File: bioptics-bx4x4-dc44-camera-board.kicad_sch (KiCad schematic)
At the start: 93 parts, among them J3 USB_C_Receptacle_USB2.0, J4 TagConnect_TC2030_SWD, U10 SRV05-4, U11 IS4xS32160F-xTL, U12 USB3300-EZK, U13 AMS1117-3.3, U14 STM32H753IITx, U9 FP6291, Y1 24MHz

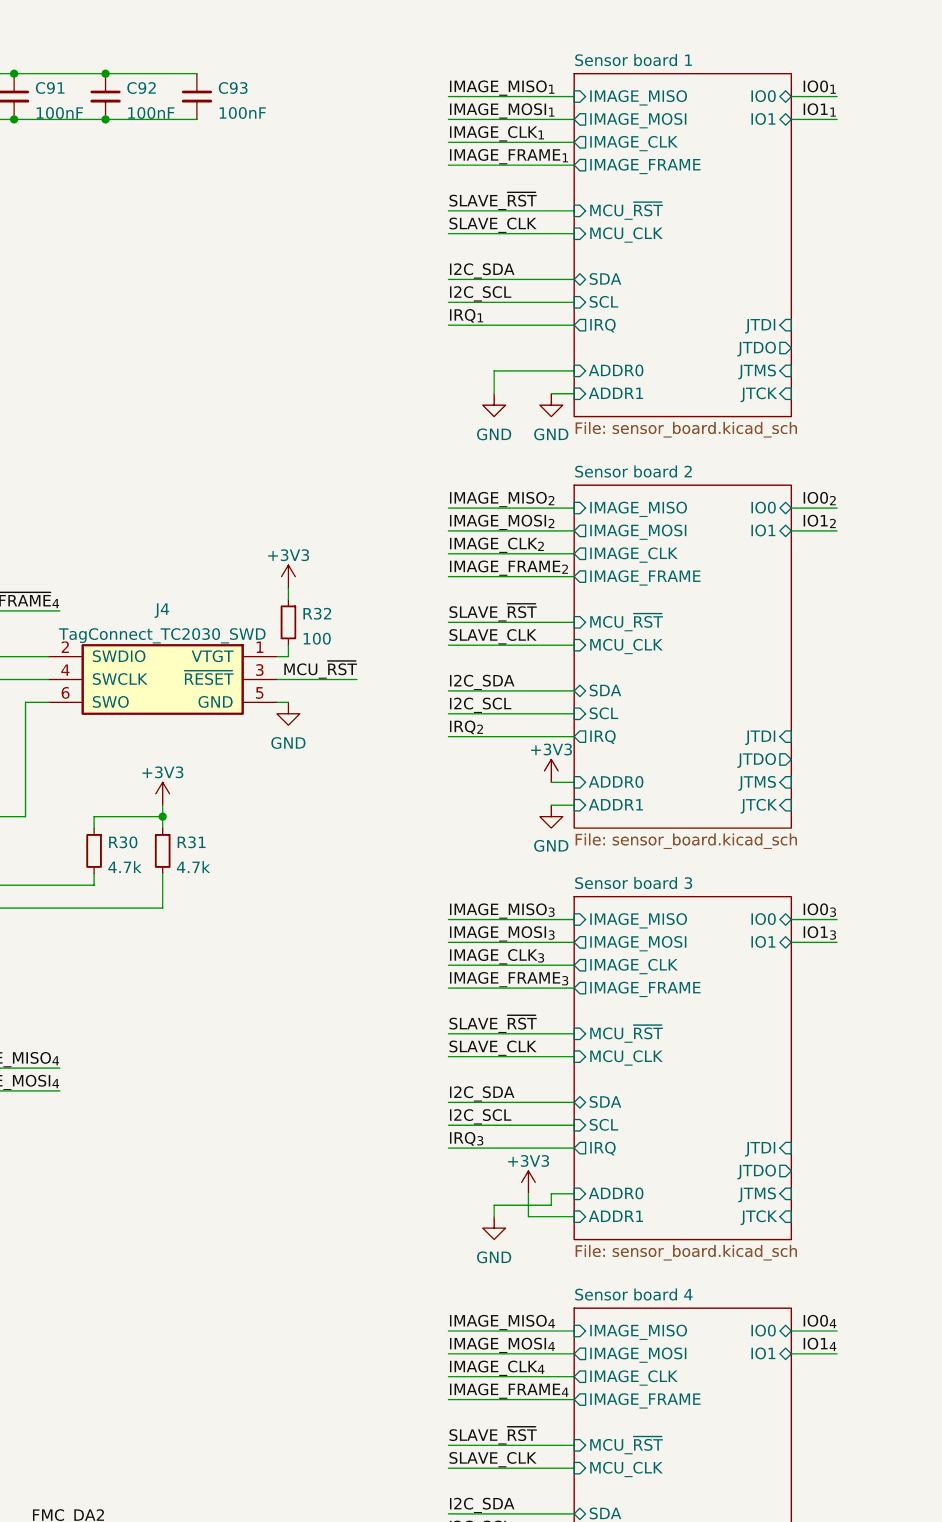
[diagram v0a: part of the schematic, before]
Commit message: Use two instead of four 3.8V voltage references
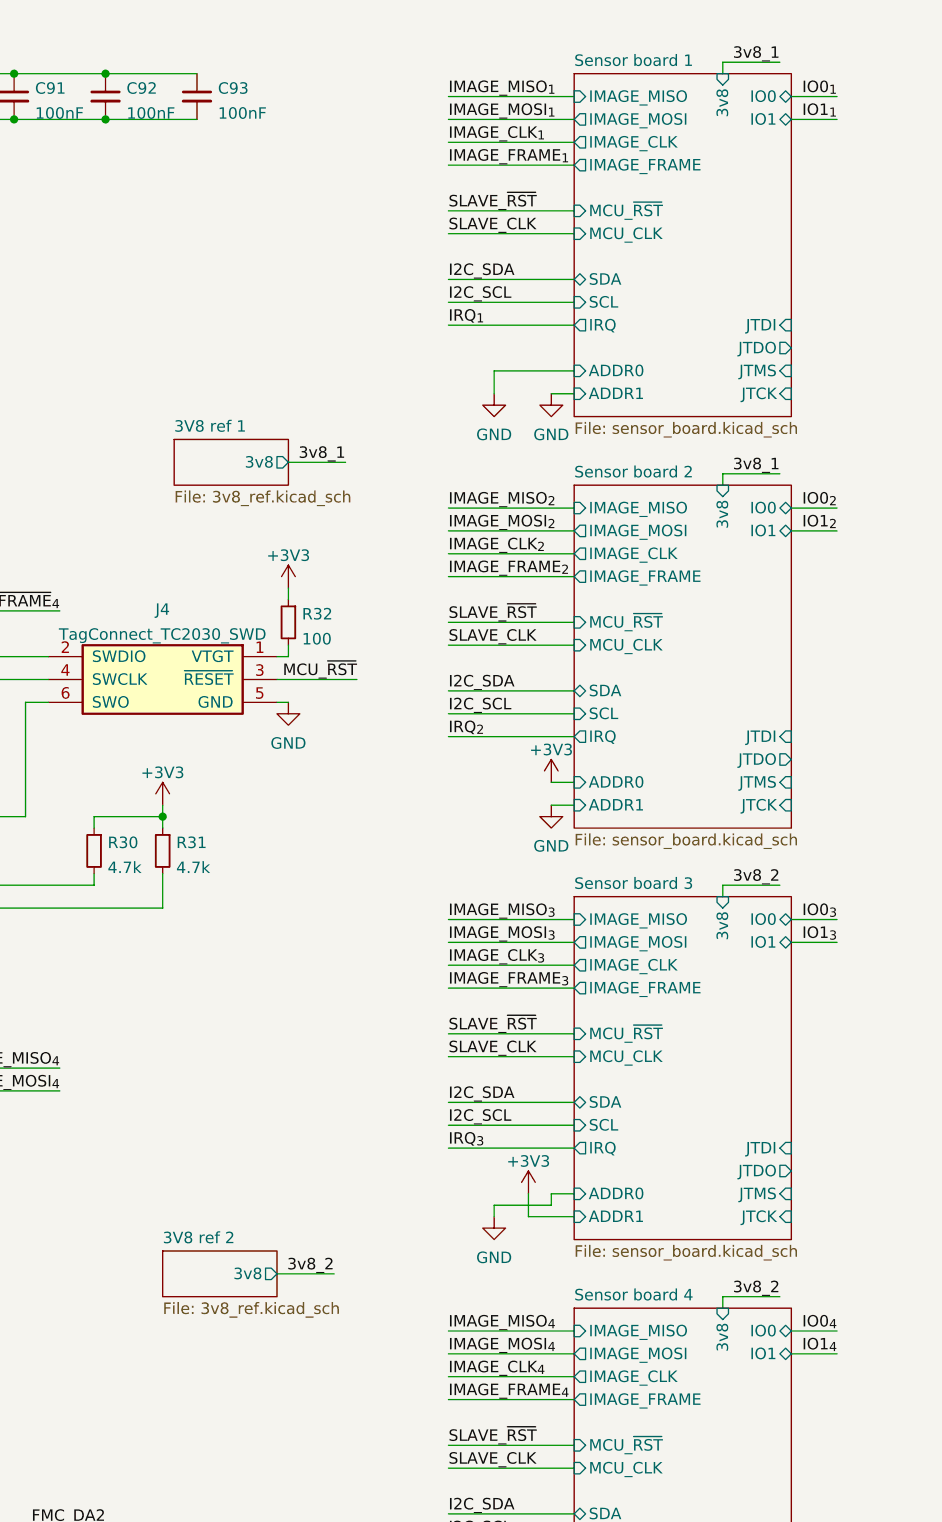
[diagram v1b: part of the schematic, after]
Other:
- added sheet 3V8 ref 1 (3v8_ref.kicad_sch)
- added sheet 3V8 ref 2 (3v8_ref.kicad_sch)
- sheet Sensor board 1 ports: added 3v8; removed none
- sheet Sensor board 2 ports: added 3v8; removed none
- sheet Sensor board 3 ports: added 3v8; removed none
- sheet Sensor board 4 ports: added 3v8; removed none

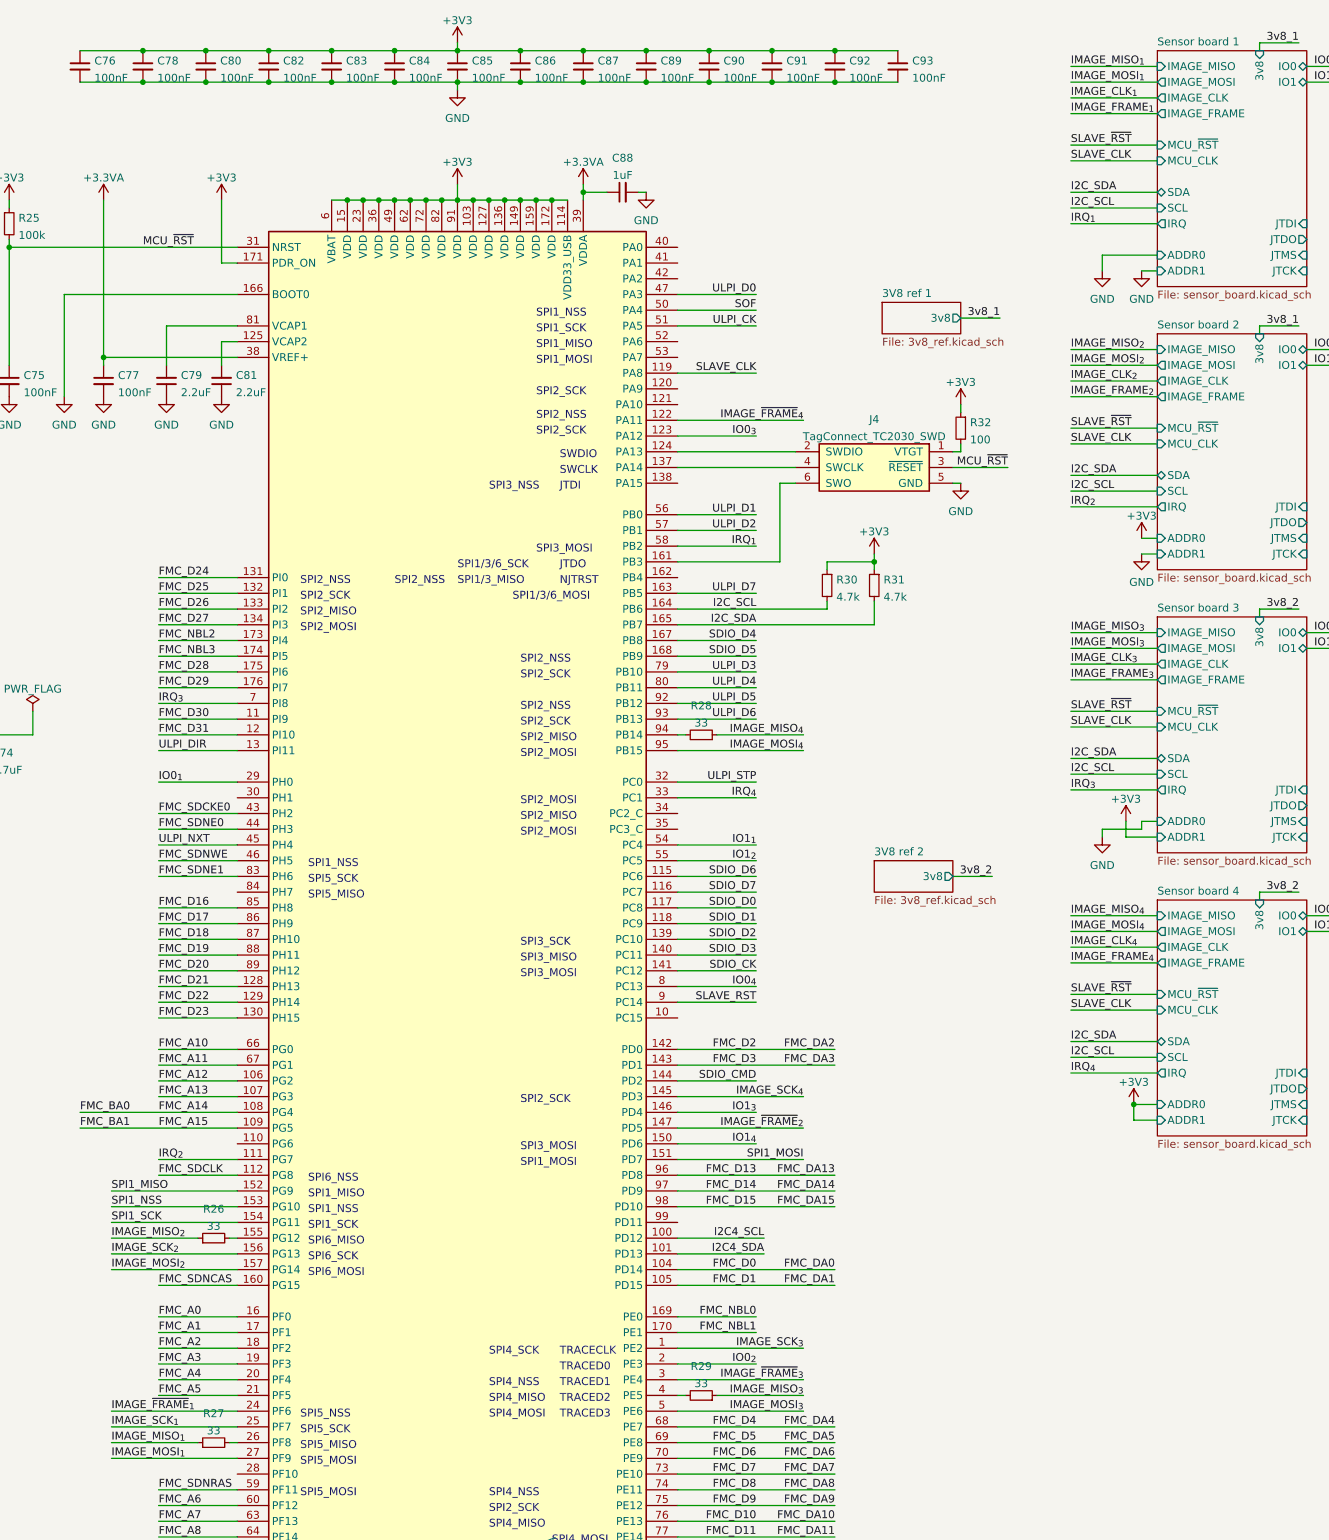
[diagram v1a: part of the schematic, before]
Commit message: Fix broken SPI net labels
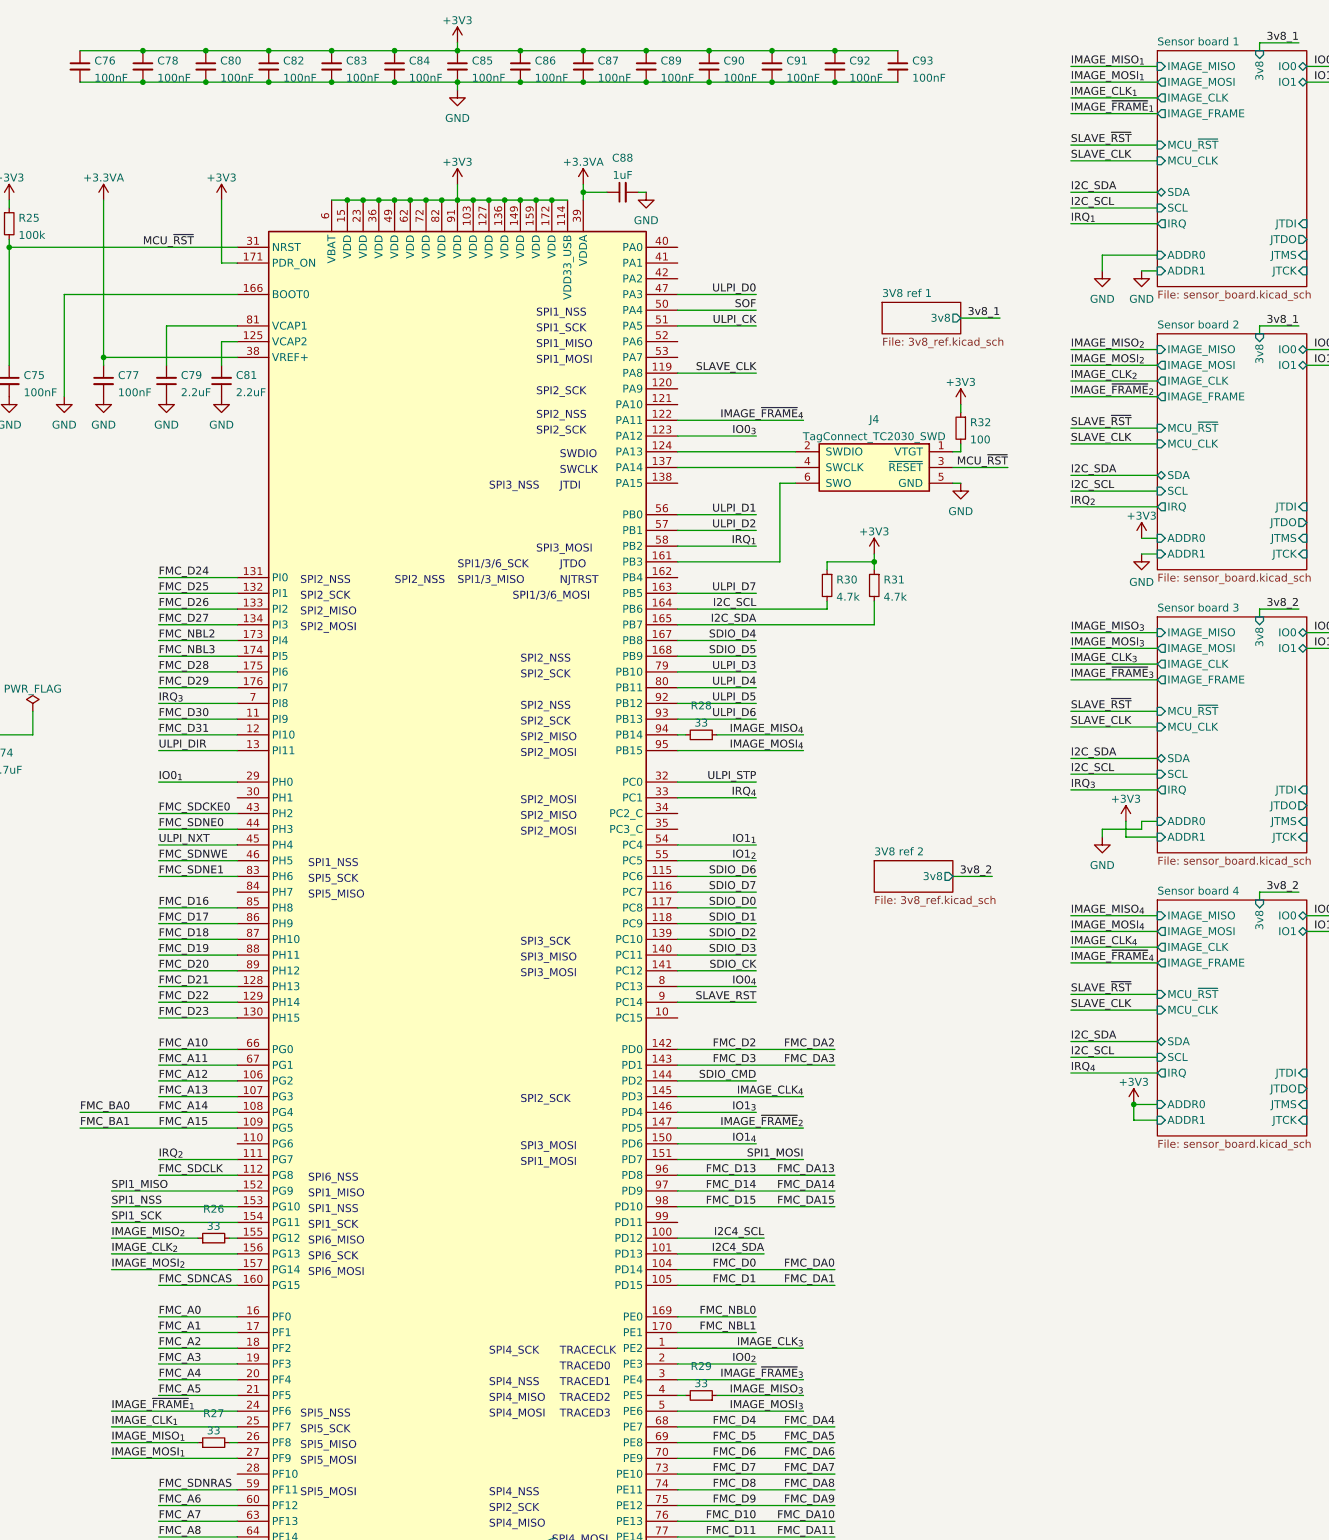
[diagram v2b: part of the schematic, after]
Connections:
- net IMAGE_SCK_{1} is gone; now on net IMAGE_CLK_{1}: U14.25 (PF7)
- net IMAGE_SCK_{2} is gone; now on net IMAGE_CLK_{2}: U14.156 (PG13)
- net IMAGE_SCK_{3} is gone; now on net IMAGE_CLK_{3}: U14.1 (PE2)
- net IMAGE_SCK_{4} is gone; now on net IMAGE_CLK_{4}: U14.145 (PD3)

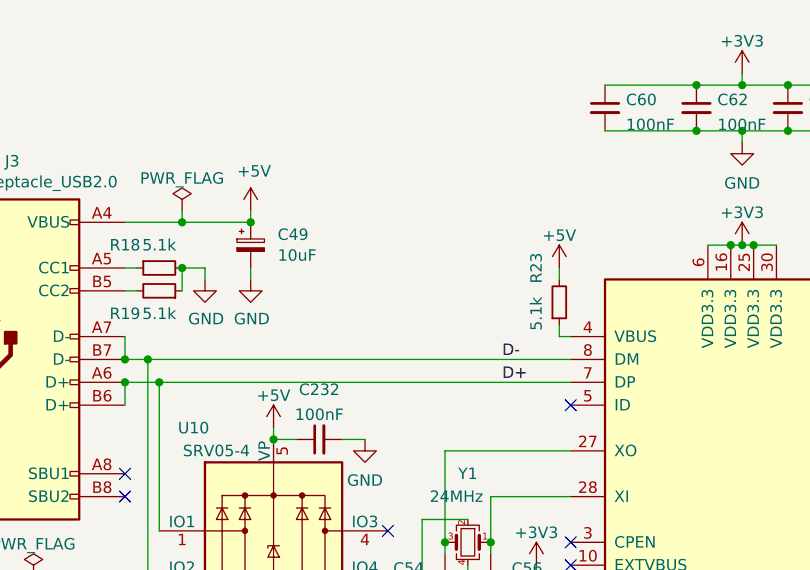
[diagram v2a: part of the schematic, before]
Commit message: Add sensor board power planes
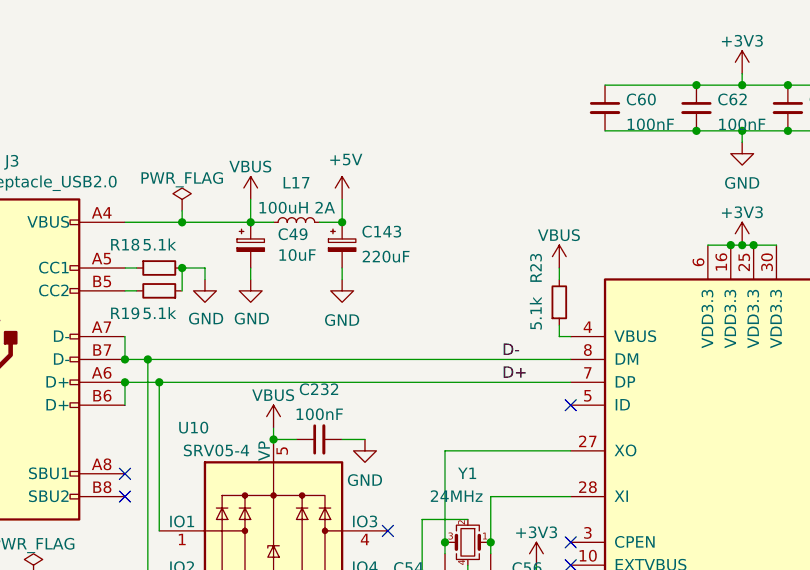
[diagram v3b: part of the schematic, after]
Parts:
- added C143: 220uF, Capacitor_SMD:CP_Elec_6.3x5.4, symbol Device:C_Polarized_Small
- added L17: 100uH 2A, Inductor_SMD:L_10.4x10.4_H4.8, symbol Device:L_Small
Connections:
- net +5V: now also C143.1, L17.2; no longer C232.1, C49.1, J3.A4 (VBUS), J3.A9 (VBUS), J3.B4 (VBUS), J3.B9 (VBUS), R23.2, U10.5 (VP)
- net GND: now also C143.2
- new net VBUS: C232.1, C49.1, J3.A4 (VBUS), J3.A9 (VBUS), J3.B4 (VBUS), J3.B9 (VBUS), L17.1, R23.2, U10.5 (VP)
